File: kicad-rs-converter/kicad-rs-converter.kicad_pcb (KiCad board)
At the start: 2 copper layers, 29 parts, among them X1 CONN_PWR, X2 CONN_RS232, X3 CONN_2

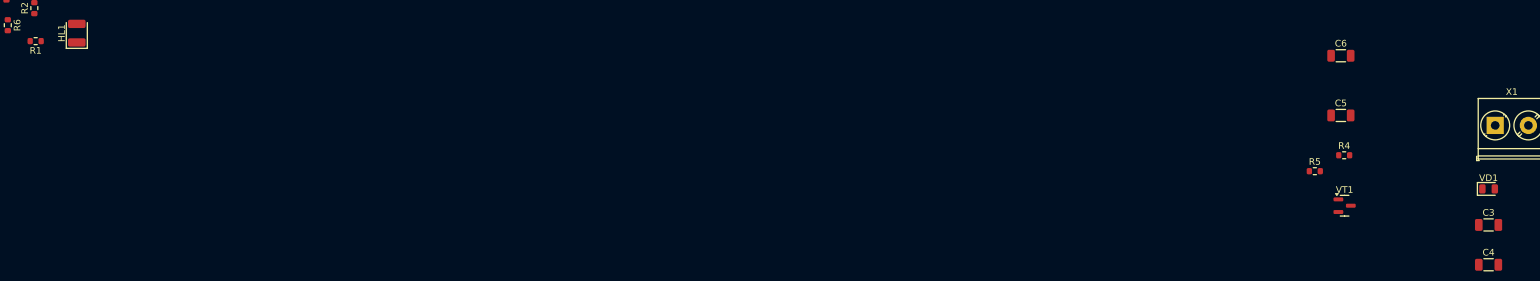
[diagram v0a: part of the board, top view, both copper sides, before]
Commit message: Assigned netclasses and colors for cicuits
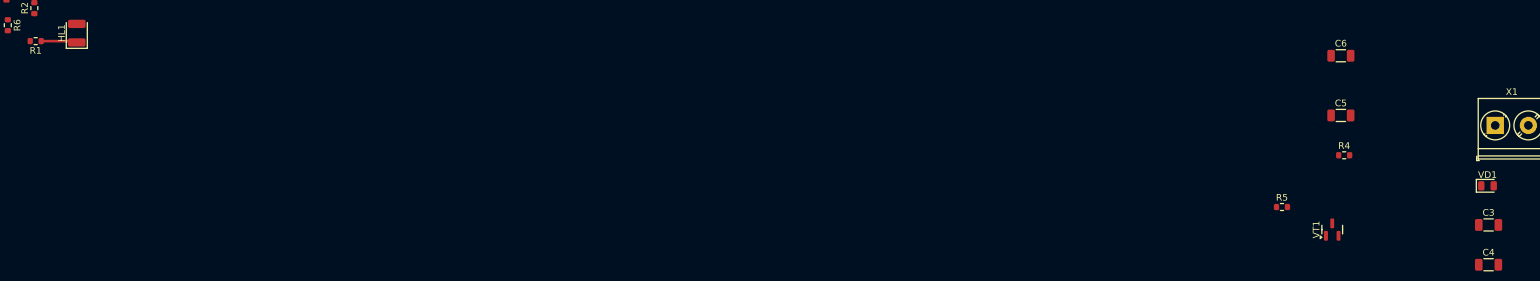
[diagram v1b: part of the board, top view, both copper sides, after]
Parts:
- moved R5 7.33 mm to (324.6, 70.8)
- moved VT1 4.05 mm to (332.2, 74.2), turned to 90 degrees
- moved VD1 0.50 mm to (355.6, 67.6)
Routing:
- net Net-(HL1-K): track 0.00 -> 5.46 mm
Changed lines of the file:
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@@
 	(footprint "Package_TO_SOT_SMD:SOT-23"
 		(layer "F.Cu")
-		(at 334.0625 70.6)
+		(at 332.2 74.2 90)
 		(descr "SOT, 3 Pin (https://www.jedec.org/system/files/docs/to-236h.pdf variant AB), generated with kicad-footprint-generator ipc_gullwing_generator.py")
 		(tags "SOT TO_SOT_SMD")
 		(property "Reference" "VT1"
-			(at 0 -2.4 0)
+			(at 0 -2.4 90)
 			(layer "F.SilkS")
 			(effects
@@
 		)
 		(property "Value" "BC807"
-			(at 0 2.4 0)
+			(at 0 2.4 90)
 			(layer "F.Fab")
 			(effects
@@
 		)
 		(property "Footprint" "Package_TO_SOT_SMD:SOT-23"
-			(at 0 0 0)
+			(at 0 0 90)
 			(unlocked yes)
 			(layer "F.Fab")
@@
 		)
 		(property "Datasheet" "https://www.onsemi.com/pub/Collateral/BC808-D.pdf"
-			(at 0 0 0)
+			(at 0 0 90)
 			(unlocked yes)
 			(layer "F.Fab")
@@
 		)
 		(property "Description" "0.8A Ic, 45V Vce, PNP Transistor, SOT-23"
-			(at 0 0 0)
+			(at 0 0 90)
 			(unlocked yes)
 			(layer "F.Fab")
@@
 		(fp_line
 			(start 0 -1.56)
-			(end -0.65 -1.56)
+			(end 0.65 -1.56)
 			(stroke
 				(width 0.12)
@@
 		(fp_line
 			(start 0 -1.56)
-			(end 0.65 -1.56)
+			(end -0.65 -1.56)
 			(stroke
 				(width 0.12)
@@
 		(fp_line
 			(start 0 1.56)
-			(end -0.65 1.56)
+			(end 0.65 1.56)
 			(stroke
 				(width 0.12)
@@
 		(fp_line
 			(start 0 1.56)
-			(end 0.65 1.56)
+			(end -0.65 1.56)
 			(stroke
 				(width 0.12)
@@
 		)
 		(fp_line
-			(start -1.92 -1.7)
-			(end -1.92 1.7)
+			(start 1.92 -1.7)
+			(end -1.92 -1.7)
 			(stroke
 				(width 0.05)
@@
 		)
 		(fp_line
-			(start -1.92 1.7)
-			(end 1.92 1.7)
+			(start -1.92 -1.7)
+			(end -1.92 1.7)
 			(stroke
 				(width 0.05)
@@
 		)
 		(fp_line
-			(start 1.92 -1.7)
-			(end -1.92 -1.7)
+			(start 1.92 1.7)
+			(end 1.92 -1.7)
 			(stroke
 				(width 0.05)
@@
 		)
 		(fp_line
-			(start 1.92 1.7)
-			(end 1.92 -1.7)
+			(start -1.92 1.7)
+			(end 1.92 1.7)
 			(stroke
 				(width 0.05)
@@
 		)
 		(fp_line
-			(start -0.65 -1.125)
-			(end -0.325 -1.45)
+			(start 0.65 -1.45)
+			(end 0.65 1.45)
 			(stroke
 				(width 0.1)
@@
 		)
 		(fp_line
-			(start -0.65 1.45)
-			(end -0.65 -1.125)
+			(start -0.325 -1.45)
+			(end 0.65 -1.45)
 			(stroke
 				(width 0.1)
@@
 		)
 		(fp_line
-			(start -0.325 -1.45)
-			(end 0.65 -1.45)
+			(start -0.65 -1.125)
+			(end -0.325 -1.45)
 			(stroke
 				(width 0.1)
@@
 		)
 		(fp_line
-			(start 0.65 -1.45)
-			(end 0.65 1.45)
+			(start 0.65 1.45)
+			(end -0.65 1.45)
 			(stroke
 				(width 0.1)
@@
 		)
 		(fp_line
-			(start 0.65 1.45)
-			(end -0.65 1.45)
+			(start -0.65 1.45)
+			(end -0.65 -1.125)
 			(stroke
 				(width 0.1)
@@
 		)
 		(fp_text user "${REFERENCE}"
-			(at 0 0 0)
+			(at 0 0 90)
 			(layer "F.Fab")
 			(effects
@@
 		)
 		(pad "1" smd roundrect
-			(at -0.9375 -0.95)
+			(at -0.9375 -0.95 90)
 			(size 1.475 0.6)
 			(layers "F.Cu" "F.Paste" "F.Mask")
@@
 		)
 		(pad "2" smd roundrect
-			(at -0.9375 0.95)
+			(at -0.9375 0.95 90)
 			(size 1.475 0.6)
 			(layers "F.Cu" "F.Paste" "F.Mask")
@@
 		)
 		(pad "3" smd roundrect
-			(at 0.9375 0)
+			(at 0.9375 0 90)
 			(size 1.475 0.6)
 			(layers "F.Cu" "F.Paste" "F.Mask")
@@
 	(footprint "Resistor_SMD:R_0603_1608Metric"
 		(layer "F.Cu")
-		(at 329.575 65.4)
+		(at 324.625 70.8)
 		(descr "Resistor SMD 0603 (1608 Metric), square (rectangular) end terminal, IPC_7351 nominal, (Body size source: IPC-SM-782 page 72, https://www.pcb-3d.com/wordpress/wp-content/uploads/ipc-sm-782a_amendment_1_and_2.pdf), generated with kicad-footprint-generator")
 		(tags "resistor")
@@
 		)
 		(property "Value" "CONN_PWR"
-			(at 2.5 6.06 0)
+			(at 2.34 5.59 0)
 			(layer "F.Fab")
 			(effects
@@
 	(footprint "Diode_SMD:D_0805_2012Metric"
 		(layer "F.Cu")
-		(at 355.76 68.07)
+		(at 355.6 67.6)
 		(descr "Diode SMD 0805 (2012 Metric), square (rectangular) end terminal, IPC_7351 nominal, (Body size source: https://docs.google.com/spreadsheets/d/1BsfQQcO9C6DZCsRaXUlFlo91Tg2WpOkGARC1WS5S8t0/edit?usp=sharing), generated with kicad-footprint-generator")
 		(tags "diode")
@@
 		)
 	)
+	(segment
+		(start 142.8 45.8)
+		(end 143 46)
+		(width 0.4)
+		(layer "F.Cu")
+		(net 20)
+	)
+	(segment
+		(start 137.625 45.8)
+		(end 142.8 45.8)
+		(width 0.4)
+		(layer "F.Cu")
+		(net 20)
+	)
 )

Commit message: Drawing edge cuts
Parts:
- moved VD1 188.0 mm to (168.6, 48.6)
- moved C3 188.0 mm to (168.8, 54.5)
- moved C4 188.0 mm to (168.8, 60.5)
- moved C5 188.0 mm to (146.5, 38.0)
- moved C6 188.0 mm to (146.5, 29.0)
- moved DA2 188.0 mm to (172.5, 69.5)
- moved R4 188.0 mm to (147.0, 44.0)
- moved R5 188.0 mm to (137.6, 51.8)
- moved VT1 188.0 mm to (145.2, 55.2)
- moved X1 188.0 mm to (169.8, 39.5)
- moved C8 100.8 mm to (146.1, 124.0), turned to 90 degrees
- moved C1 98.0 mm to (152.1, 124.1)
- moved C7 97.9 mm to (146.1, 130.1), turned to 90 degrees
- moved C2 97.5 mm to (152.1, 129.6)
- moved R11 95.2 mm to (179.9, 127.7), turned to 180 degrees
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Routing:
- net Net-(HL1-K): track 5.46 -> 0.28 mm
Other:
- board outline added: 75 x 50 mm

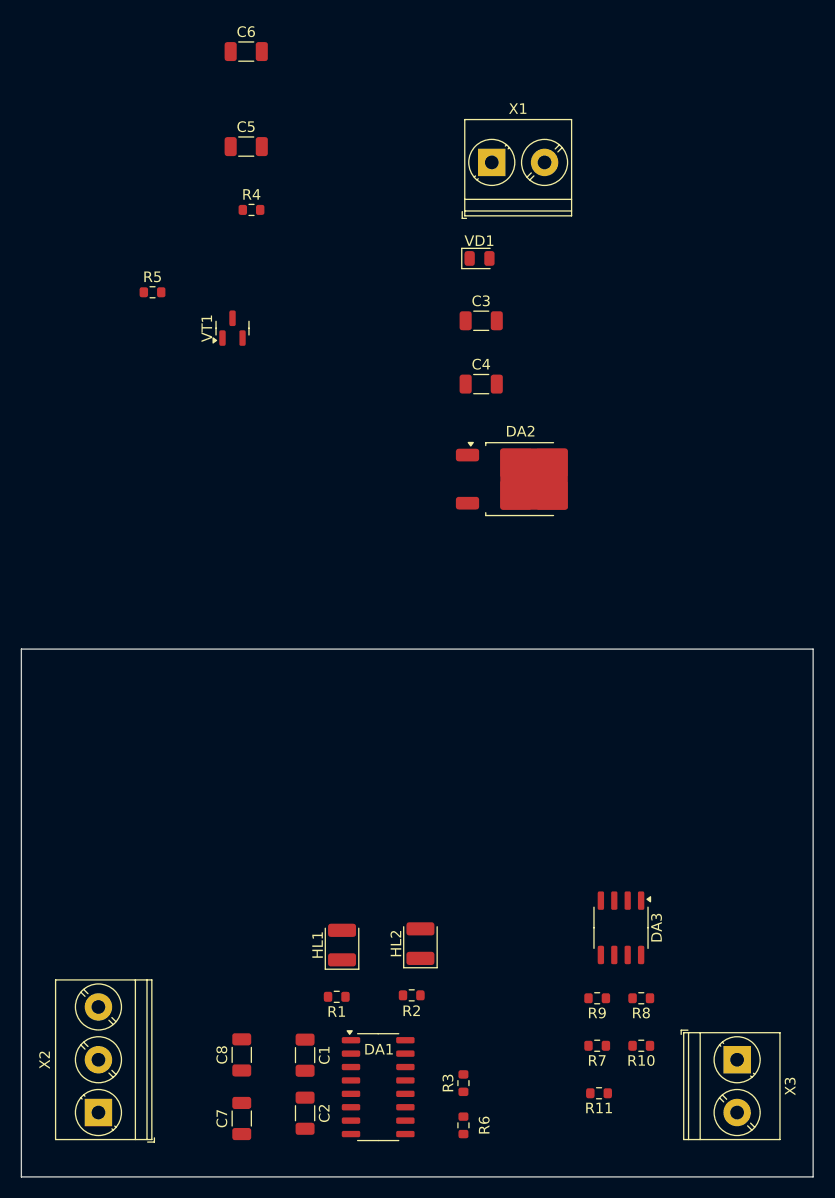
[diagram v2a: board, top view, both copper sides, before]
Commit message: PCBdoc: everything connected except for GND and +5V
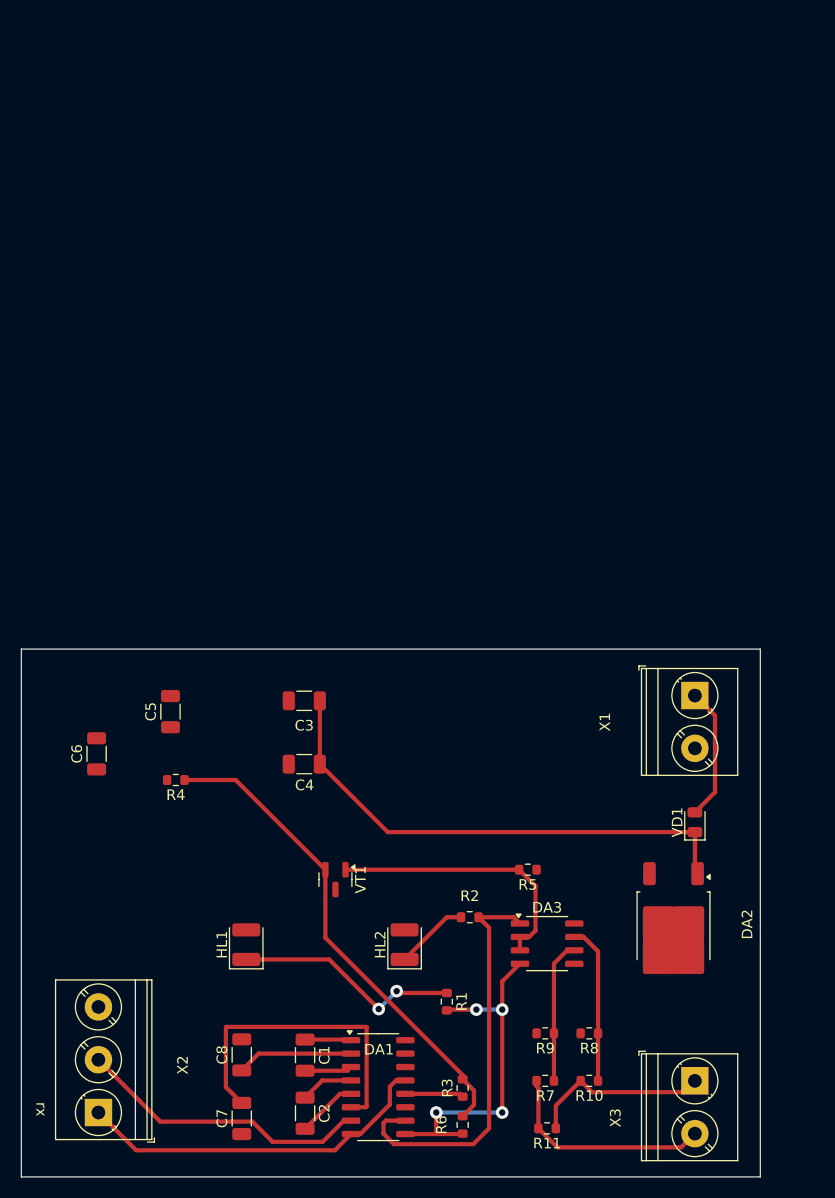
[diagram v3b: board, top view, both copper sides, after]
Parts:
- moved C6 68.0 mm to (132.3, 95.5), turned to 90 degrees
- moved R5 65.2 mm to (173.2, 106.5), turned to 180 degrees
- moved VD1 57.2 mm to (189.0, 102.0), turned to 90 degrees
- moved R4 54.5 mm to (139.8, 98.0), turned to 180 degrees
- moved X1 54.0 mm to (189.0, 90.0), turned to -90 degrees
- moved C5 54.0 mm to (139.3, 91.5), turned to 90 degrees
- moved VT1 53.1 mm to (154.9, 107.4), turned to -90 degrees
- moved DA2 44.8 mm to (187.0, 111.9), turned to -90 degrees
- moved C3 39.7 mm to (152.0, 90.5), turned to 180 degrees
- moved C4 39.7 mm to (152.0, 96.5), turned to 180 degrees
- moved R1 10.4 mm to (165.5, 119.0), turned to -90 degrees
- moved R2 9.22 mm to (167.7, 111.0), turned to 0 degrees
- moved HL1 9.08 mm to (146.5, 113.6)
- moved DA3 7.16 mm to (175.0, 113.5), turned to 0 degrees
- moved R7 5.94 mm to (174.8, 126.5)
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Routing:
- net Net-(DA2-VI): track 0.00 -> 48.2 mm
- net Net-(VT1-E): track 0.00 -> 46.5 mm
- net Net-(DA1-TXIN2): track 0.00 -> 38.8 mm
- net Net-(DA1-RXIN1): track 0.00 -> 34.3 mm
- net Net-(DA1-~{RXOUT2}): track 0.00 -> 33.8 mm, vias 0 -> 4
- net Net-(DA1-V-): track 0.00 -> 30.2 mm
- net Net-(DA1-~{TXOUT2}): track 0.00 -> 28.0 mm
- net Net-(DA3-DE): track 0.00 -> 25.9 mm
- net Net-(HL1-K): track 0.28 -> 21.7 mm, vias 0 -> 2
- net Net-(R11-Pad2): track 0.00 -> 20.7 mm
- net Net-(R10-Pad2): track 0.00 -> 17.2 mm
- net Net-(DA3-BZ): track 0.00 -> 15.1 mm
- net Net-(DA3-AY): track 0.00 -> 13.6 mm
- net Net-(VD1-A): track 0.00 -> 12.6 mm
- net Net-(DA1-V+): track 0.00 -> 11.0 mm
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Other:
- board size 75 x 50 mm -> 70 x 50 mm
- board text added: "rx"

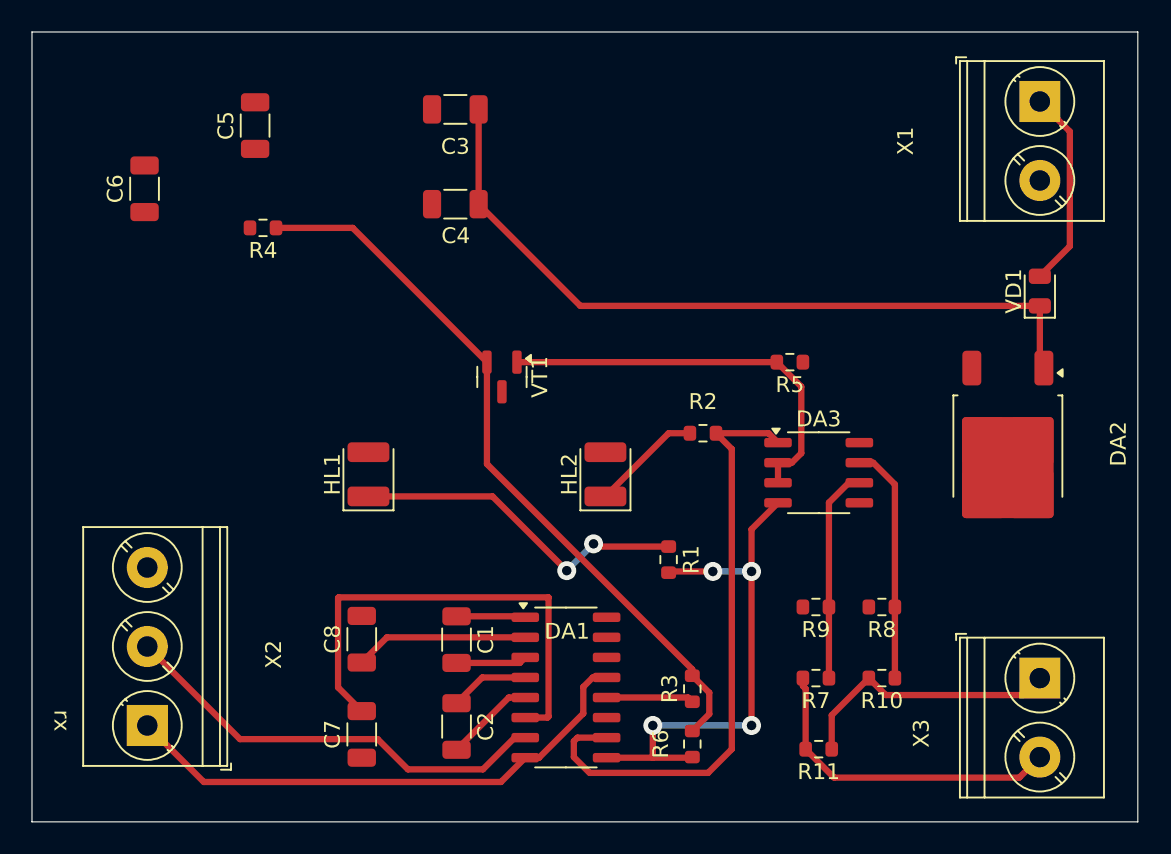
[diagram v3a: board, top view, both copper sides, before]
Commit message: pcbdoc finished, but some parts can be done better.
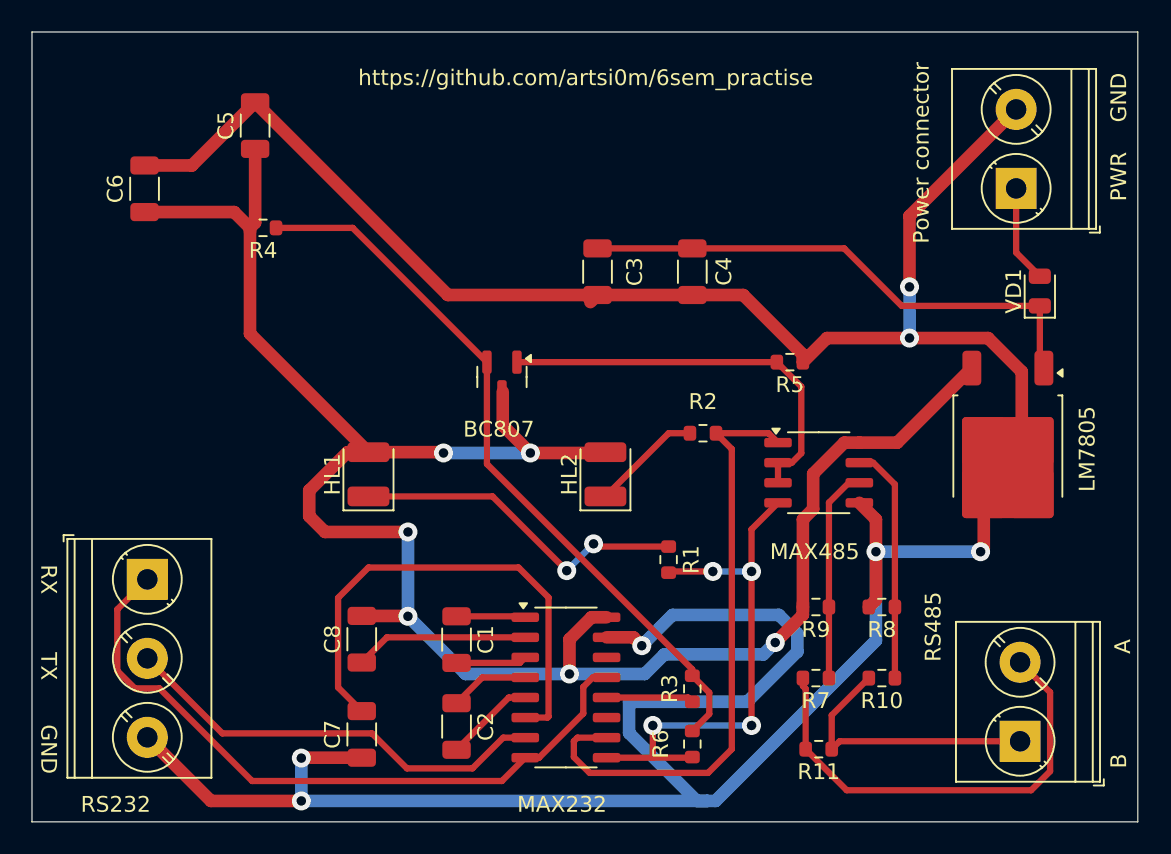
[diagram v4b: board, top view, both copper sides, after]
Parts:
- Power connector: renamed from X1
- moved C4 15.6 mm to (167.0, 100.8), turned to -90 degrees
- moved C3 13.7 mm to (161.0, 100.8), turned to -90 degrees
- moved RS232 9.25 mm to (132.5, 120.2), turned to -90 degrees
- moved Power connector 5.70 mm to (187.5, 95.5), turned to 90 degrees
- moved RS485 4.19 mm to (187.8, 130.5), turned to 90 degrees
- renumbered VT1 to BC807, DA2 to LM7805, DA1 to MAX232, DA3 to MAX485, X2 to RS232, X3 to RS485
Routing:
- net GND: track 0.00 -> 208.9 mm, vias 0 -> 7
- net +5V: track 0.00 -> 125.7 mm, vias 0 -> 6
- net Net-(DA2-VI): track 48.2 -> 33.5 mm
- net Net-(DA1-RXIN1): track 34.3 -> 44.1 mm
- net Net-(R11-Pad2): track 20.7 -> 29.3 mm
- net Net-(VD1-A): track 12.6 -> 6.18 mm
- net Net-(DA1-V-): track 30.2 -> 31.7 mm
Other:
- board text added: "A"
- board text added: "B"
- board text added: "GND"
- board text added: "PWR"
- board text added: "RX"
- board text added: "TX"
- board text added: "https://github.com/artsi0m/6sem_practise"
- board text removed: "rx"
